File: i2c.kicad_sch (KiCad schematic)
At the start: 22 parts, among them U16 PCA9517ADP, U23 TS5A3359_VSSOP, U24 TS5A3359_VSSOP

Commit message: [#65754] Rename project
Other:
- title: SO-DIMM DDR5 Tester -> RDIMM DDR5 Tester

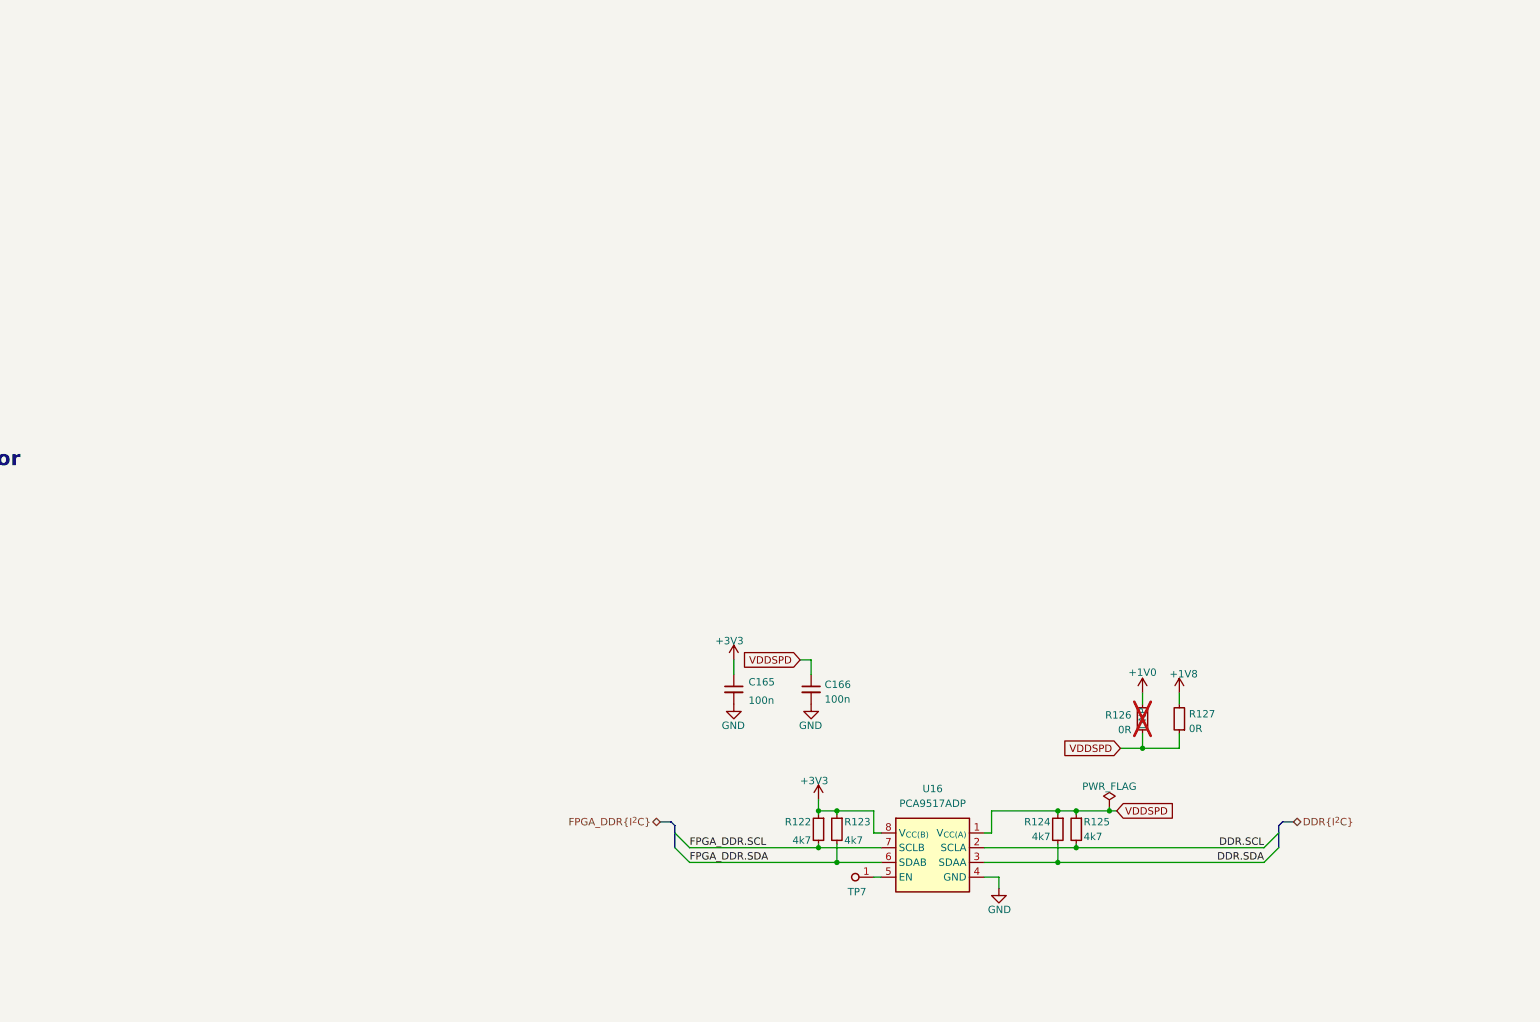
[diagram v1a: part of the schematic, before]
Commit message: [#67402] Add I3C circuit, update I2C DDR
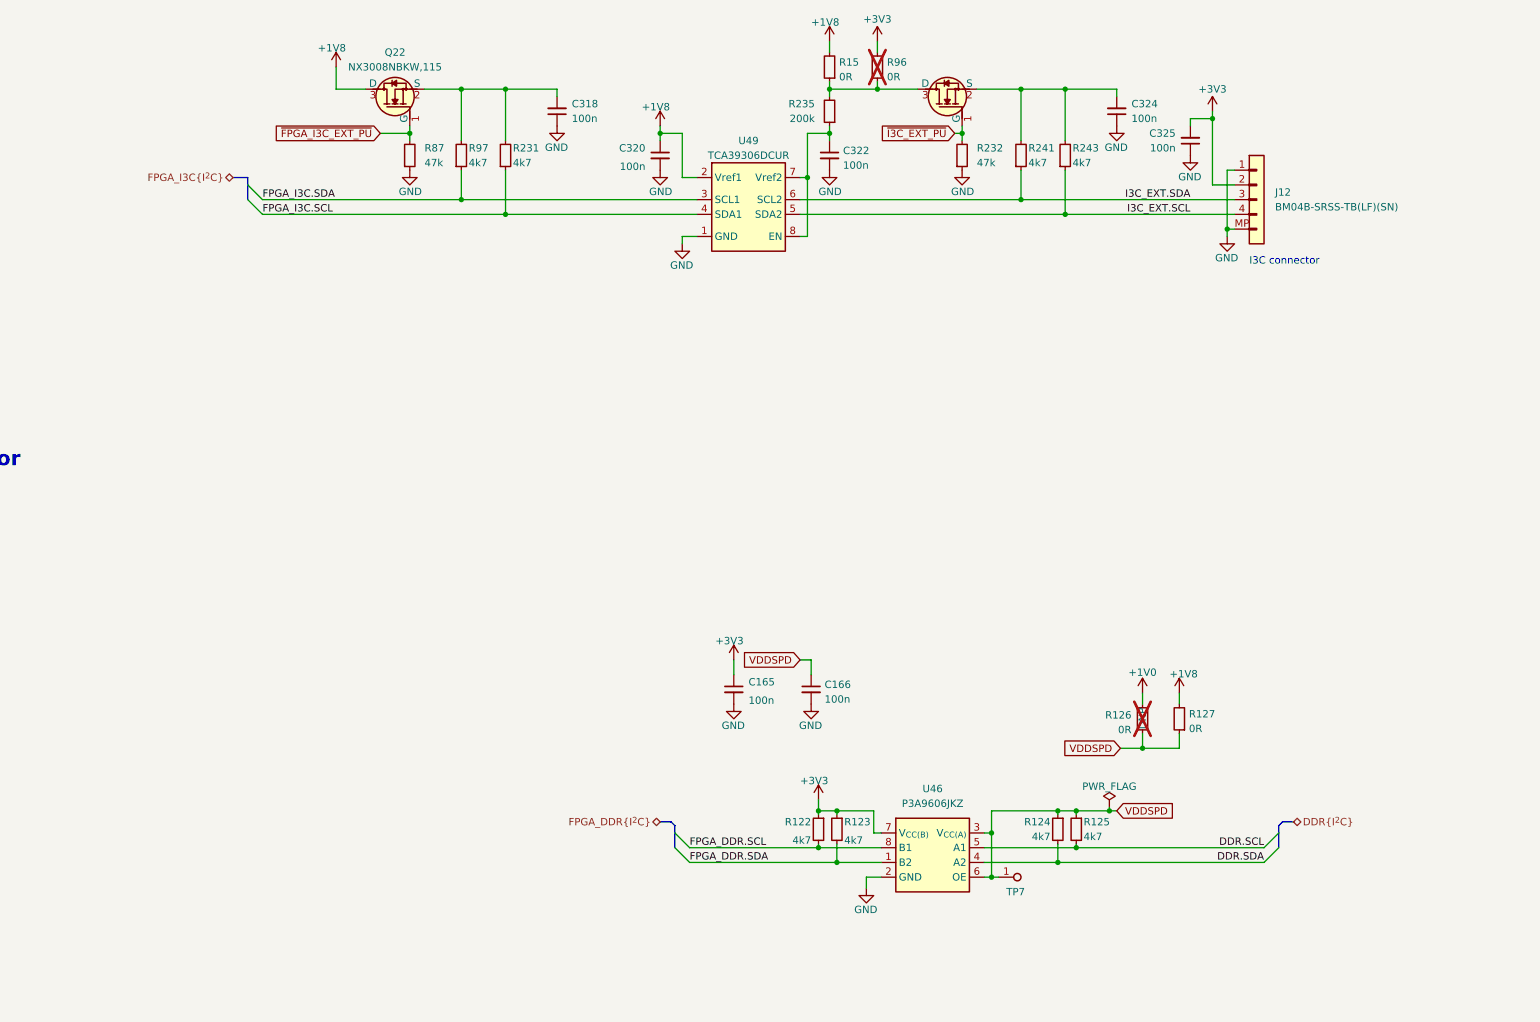
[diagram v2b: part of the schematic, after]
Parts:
- removed U16: PCA9517ADP, antmicro-footprints:TSSOP-8_3x3mm_P0.65mm, symbol antmicroLogicTranslatorsLevelShifters:PCA9517ADP
- added C318, C320, C322, C324, C325: C_100n_0402, antmicro-footprints:C_0402_1005Metric, symbol antmicroCapacitors0402:C_100n_0402
- added J12: JST_SH_1x4_BM04B-SRSS-TB-LF-SN, antmicro-footprints:Conn_JST_SH_1x4_BM04B-SRSS-TB-LF-SN, symbol antmicroWire2BoardConnectors:JST_SH_1x4_BM04B-SRSS-TB-LF-SN
- added Q22, Q24: NX3008NBKW, antmicro-footprints:SOT-323, symbol antmicroTransistorsFETsMOSFETsSingle:NX3008NBKW
- added R15, R96: R_0R_0402, antmicro-footprints:R_0402_1005Metric, symbol antmicroResistors0402:R_0R_0402
- added R231, R241, R243, R97: R_4k7_0402, antmicro-footprints:R_0402_1005Metric, symbol antmicroResistors0402:R_4k7_0402
- added R232, R87: R_47k_0402, antmicro-footprints:R_0402_1005Metric, symbol antmicroResistors0402:R_47k_0402
- added R235: R_200k_0402, antmicro-footprints:R_0402_1005Metric, symbol antmicroResistors0402:R_200k_0402
- added U46: P3A9606JKZ, antmicro-footprints:X2SON8_1.4x1x0.32mm_P0.35mm, symbol antmicroLogicTranslatorsLevelShifters:P3A9606JK
- added U49: TCA39306_VSSOP, antmicro-footprints:VSSOP-8_2.3x2mm_P0.5mm, symbol antmicroLogicTranslatorsLevelShifters:TCA39306_VSSOP
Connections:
- net +1V8: now also C320.1, Q22.3 (D), R15.2, U49.2 (Vref1)
- net +3V3: now also C325.2, J12.2, R96.2, U46.7 (V_{CC(B)})
- net DDR.SCL: now also U46.5 (A1)
- net DDR.SDA: now also U46.4 (A2)
- net FPGA_DDR.SCL: now also U46.8 (B1)
- net FPGA_DDR.SDA: now also U46.1 (B2)
- net GND: now also C318.1, C320.2, C322.2, C324.1, C325.1, J12.1, J12.MP, R232.1, R87.1, U46.2 (GND), U49.1 (GND)
- net VDDSPD: now also TP7.1, U46.3 (V_{CC(A)}), U46.6 (OE)
- new net: C324.2, Q24.2 (S), R241.2, R243.2
- new net: C322.1, R235.1, U49.7 (Vref2), U49.8 (EN)
- new net: Q24.3 (D), R15.1, R235.2, R96.1
- new net: C318.2, Q22.2 (S), R231.2, R97.2
- new net FPGA_I3C.SCL: R231.1, U49.4 (SDA1)
- new net FPGA_I3C.SDA: R97.1, U49.3 (SCL1)
- new net I3C_EXT.SCL: J12.4, R243.1, U49.5 (SDA2)
- new net I3C_EXT.SDA: J12.3, R241.1, U49.6 (SCL2)
- new net ~{FPGA_I3C_EXT_PU}: Q22.1 (G), R87.2
- new net ~{I3C_EXT_PU}: Q24.1 (G), R232.2
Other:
- note added: "I3C connector"
- moved on the sheet: TP7

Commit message: [#67725] Update I2C sheet
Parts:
- removed U46: P3A9606JKZ, antmicro-footprints:X2SON8_1.4x1x0.32mm_P0.35mm, symbol antmicroLogicTranslatorsLevelShifters:P3A9606JK
- added U33: TPD4E05U06QDQARQ1, antmicro-footprints:USON-10_2.5x1mm_P0.5mm, symbol antmicroTVSDiodes:TPD4E05U06QDQARQ1
- added U45: TCA39306_VSSOP, antmicro-footprints:VSSOP-8_2.3x2mm_P0.5mm, symbol antmicroLogicTranslatorsLevelShifters:TCA39306_VSSOP
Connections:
- net +3V3: now also U33.1, U33.10, U45.2 (Vref1)
- net DDR.SCL: now also U45.6 (SCL2)
- net DDR.SDA: now also U45.5 (SDA2)
- net FPGA_DDR.SCL: now also U45.3 (SCL1)
- net FPGA_DDR.SDA: now also U45.4 (SDA1)
- net GND: now also U33.3, U33.8, U45.1 (GND)
- net I3C_EXT.SCL: now also U33.4, U33.7
- net I3C_EXT.SDA: now also U33.2, U33.9
- net VDDSPD: now also U45.7 (Vref2), U45.8 (EN)
- new net: U33.5, U33.6
- no-connect marks 0 -> 1
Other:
- note added: "I3C"
- moved on the sheet: C165, C166, C318, C320, C322, C324, C325, J12, Q22, R122, R123, R124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

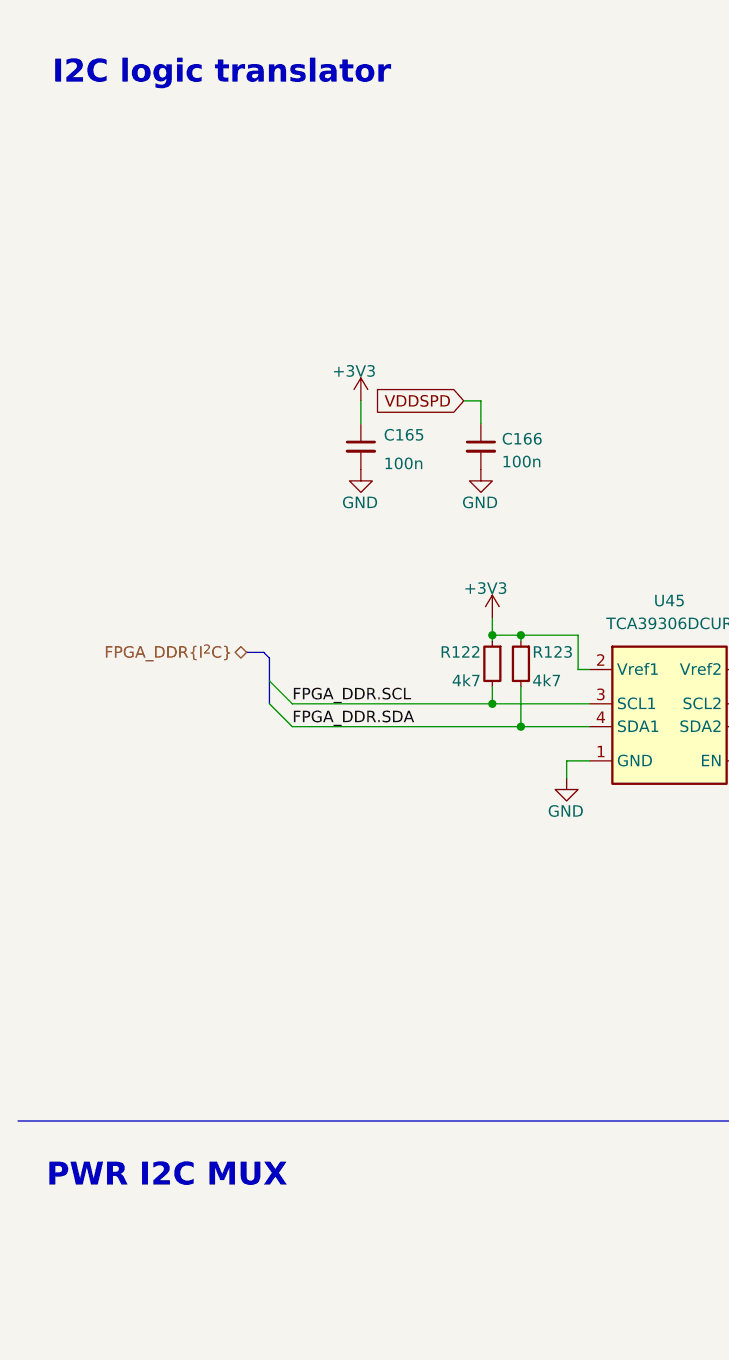
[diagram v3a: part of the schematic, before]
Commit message: [#67725] Connect I3C signals to the FPGA
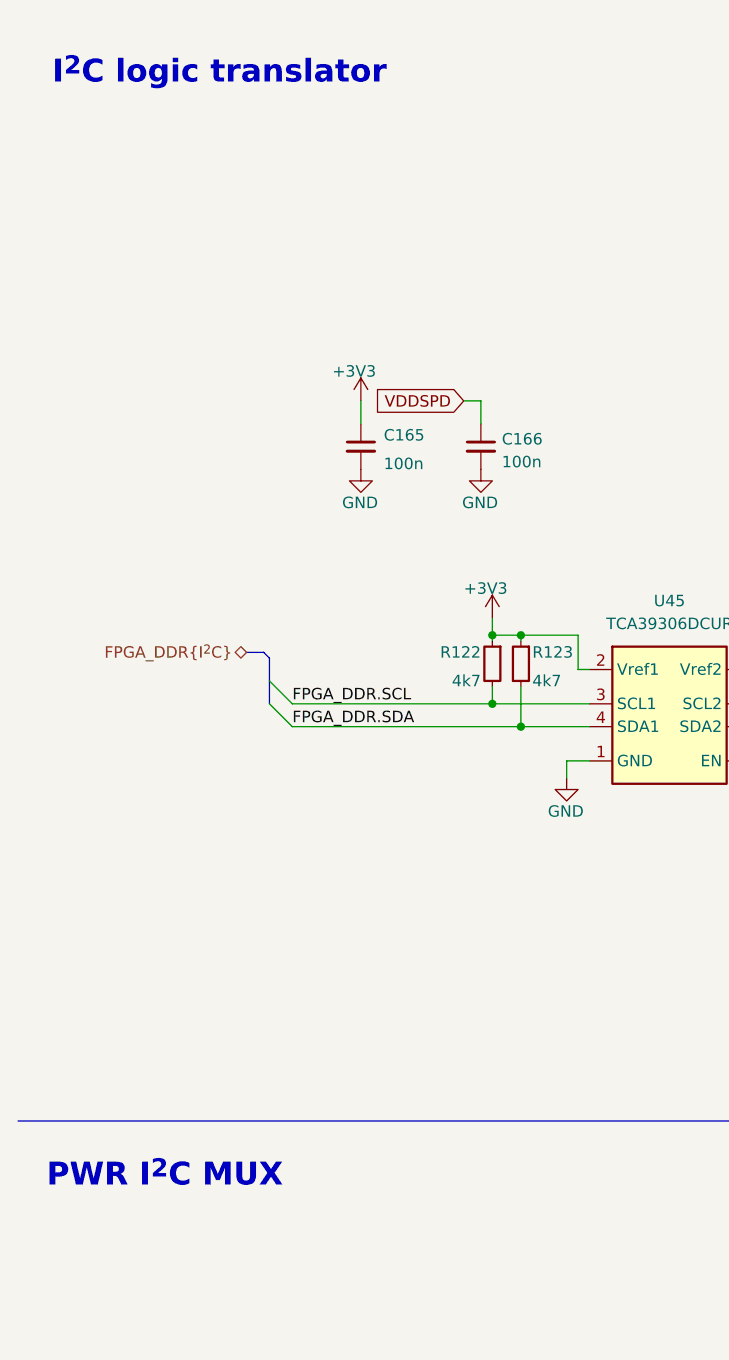
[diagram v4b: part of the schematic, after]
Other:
- note added: "I^{2}C logic translator"
- note added: "PWR I^{2}C MUX"
- note removed: "I2C logic translator"
- note removed: "PWR I2C MUX"
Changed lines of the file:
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@@
     (effects (font (size 1.27 1.27)) (justify left bottom))
   )
-  (text "PWR I2C MUX" (at 15.24 142.24 0)
+  (text "PWR I^{2}C MUX" (at 15.24 142.24 0)
     (effects (font (size 2.54 2.54) (thickness 0.4978) bold) (justify left bottom))
   )
@@
     (effects (font (size 1.27 1.27) (thickness 0.254) bold) (justify left bottom))
   )
-  (text "I2C logic translator" (at 15.875 19.685 0)
+  (text "I^{2}C logic translator" (at 15.875 19.685 0)
     (effects (font (size 2.54 2.54) (thickness 0.4978) bold) (justify left bottom))
   )

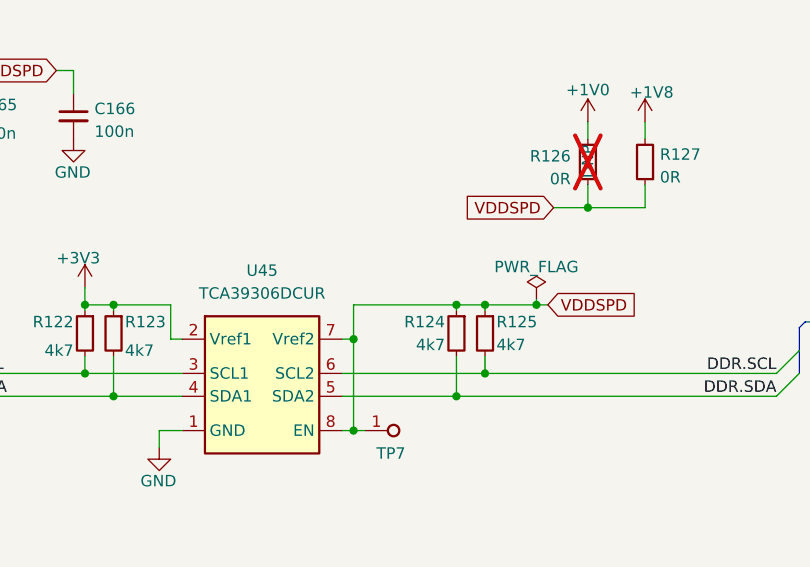
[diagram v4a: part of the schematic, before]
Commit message: [#67725] Import review changes to PCB. Minor schematic fix
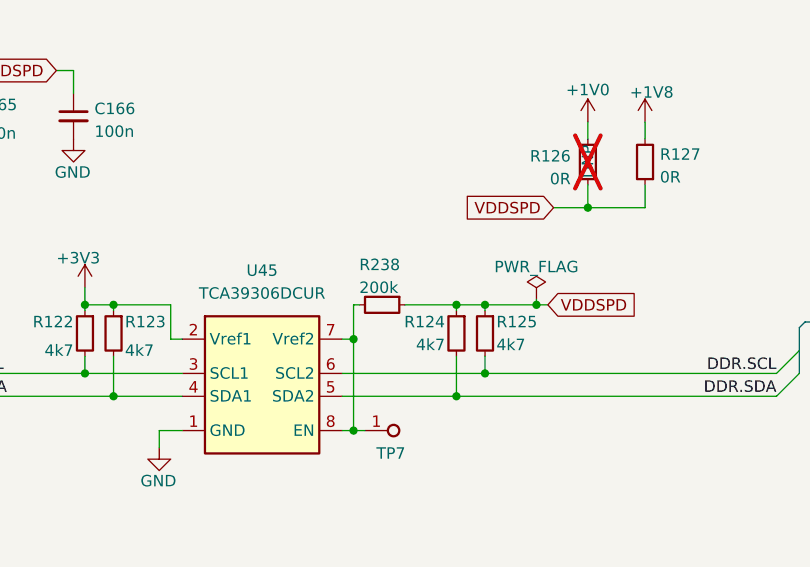
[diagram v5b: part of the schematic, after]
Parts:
- added R238: R_200k_0402, antmicro-footprints:R_0402_1005Metric, symbol antmicroResistors0402:R_200k_0402
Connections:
- net VDDSPD: now also R238.1; no longer TP7.1, U45.7 (Vref2), U45.8 (EN)
- new net: R238.2, TP7.1, U45.7 (Vref2), U45.8 (EN)
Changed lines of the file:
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@@
     (stroke (width 0) (type default))
   )
-  (wire (pts (xy 94.615 80.645) (xy 106.045 80.645))
+  (wire (pts (xy 94.615 80.645) (xy 95.25 80.645))
     (stroke (width 0) (type default))
   )
@@
   )
   (wire (pts (xy 171.45 223.52) (xy 171.45 224.79))
+    (stroke (width 0) (type default))
+  )
+  (wire (pts (xy 100.33 80.645) (xy 106.045 80.645))
     (stroke (width 0) (type default))
   )
@@
         )
       )
+    )
+  )
+  (symbol (lib_id "antmicroResistors0402:R_200k_0402") (at 100.33 80.645 0) (mirror y) (unit 1)
+    (in_bom yes) (on_board yes) (dnp no)
+    (property "Reference" "R238" (at 95.25 76.2 0)
+      (effects (font (size 1.27 1.27) (thickness 0.15)) (justify right))
+    )
+    (property "Value" "R_200k_0402" (at 80.01 93.345 0)
+      (effects (font (size 1.27 1.27) (thickness 0.15)) (justify left bottom) hide)
+    )
+    (property "Footprint" "antmicro-footprints:R_0402_1005Metric" (at 80.01 95.885 0)
+      (effects (font (size 1.27 1.27) (thickness 0.15)) (justify left bottom) hide)
+    )
+    (property "Datasheet" "https://www.bourns.com/docs/product-datasheets/cr.pdf" (at 80.01 98.425 0)
+      (effects (font (size 1.27 1.27) (thickness 0.15)) (justify left bottom) hide)
+    )
+    (property "MPN" "CR0402-FX-2003GLF" (at 80.01 100.965 0)
+      (effects (font (size 1.27 1.27) (thickness 0.15)) (justify left bottom) hide)
+    )
+    (property "Manufacturer" "Bourns" (at 80.01 103.505 0)
+      (effects (font (size 1.27 1.27) (thickness 0.15)) (justify left bottom) hide)
+    )
+    (property "License" "Apache-2.0" (at 80.01 106.045 0)
+      (effects (font (size 1.27 1.27) (thickness 0.15)) (justify left bottom) hide)
+    )
+    (property "Author" "Antmicro" (at 80.01 108.585 0)
+      (effects (font (size 1.27 1.27) (thickness 0.15)) (justify left bottom) hide)
+    )
+    (property "Val" "200k" (at 95.25 78.74 0)
+      (effects (font (size 1.27 1.27) (thickness 0.15)) (justify right))
+    )
+    (property "Tolerance" "1%" (at 80.01 90.805 0)
+      (effects (font (size 1.27 1.27)) (justify left bottom) hide)
+    )
+    (pin "1")
+    (pin "2")
+    (instances
+      (project "data-center-rdimm-ddr5-tester"
+        (path "/1faa6543-e26a-4449-8bac-ee14b9f19e5f/3f0d6799-172b-44a7-b59e-98d6f5f3049b"
+          (reference "R238") (unit 1)
+        )
+      )

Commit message: [#68016] Revert I2C translator to PCA9517ADP
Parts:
- removed R238: R_200k_0402, antmicro-footprints:R_0402_1005Metric, symbol antmicroResistors0402:R_200k_0402
- removed U45: TCA39306_VSSOP, antmicro-footprints:VSSOP-8_2.3x2mm_P0.5mm, symbol antmicroLogicTranslatorsLevelShifters:TCA39306_VSSOP
- added U45: PCA9517ADP, antmicro-footprints:TSSOP-8_3x3mm_P0.65mm, symbol antmicroLogicTranslatorsLevelShifters:PCA9517ADP
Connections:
- net +3V3: now also U45.8 (V_{CC(B)})
- net DDR.SCL: now also U45.2 (SCLA)
- net DDR.SDA: now also U45.3 (SDAA)
- net FPGA_DDR.SCL: now also U45.7 (SCLB)
- net FPGA_DDR.SDA: now also U45.6 (SDAB)
- net GND: now also U45.4 (GND)
- net VDDSPD: now also U45.1 (V_{CC(A)})
- net at TP7.1: now also U45.5 (EN)
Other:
- moved on the sheet: C165, C166, C318, C320, C322, C324, C325, J12, Q22, Q24, R122, R123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

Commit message: [#68016] Clean-up the schematic
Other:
- note added: "I^{2}C"
- note removed: "I^{2}C logic translator"
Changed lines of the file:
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@@
   (title_block
     (title "RDIMM DDR5 Tester")
-    (date "2024-09-26")
+    (date "2024-10")
     (rev "2.0.0")
     (comment 1 "www.antmicro.com")
@@
   )
   (text "PWR I^{2}C MUX" (at 15.24 142.24 0)
-    (effects (font (size 2.54 2.54) (thickness 0.4978) bold) (justify left bottom))
+    (effects (font (size 2 2) (thickness 0.4978) bold) (justify left bottom))
   )
   (text "L" (at 160.02 241.3 0)
@@
   )
   (text "I3C" (at 175.895 19.685 0)
-    (effects (font (size 2.54 2.54) (thickness 0.4978) bold) (justify left bottom))
+    (effects (font (size 3 3) (thickness 0.6) bold) (justify left bottom))
   )
   (text "H" (at 163.83 241.3 0)
@@
     (effects (font (size 1.27 1.27) (thickness 0.254) bold) (justify left bottom))
   )
-  (text "I^{2}C logic translator" (at 15.875 19.685 0)
-    (effects (font (size 2.54 2.54) (thickness 0.4978) bold) (justify left bottom))
+  (text "I^{2}C" (at 15.875 19.685 0)
+    (effects (font (size 3 3) (thickness 0.6) bold) (justify left bottom))
   )
   (text "H" (at 163.83 243.84 0)
